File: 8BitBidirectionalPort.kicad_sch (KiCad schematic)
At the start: 4 parts

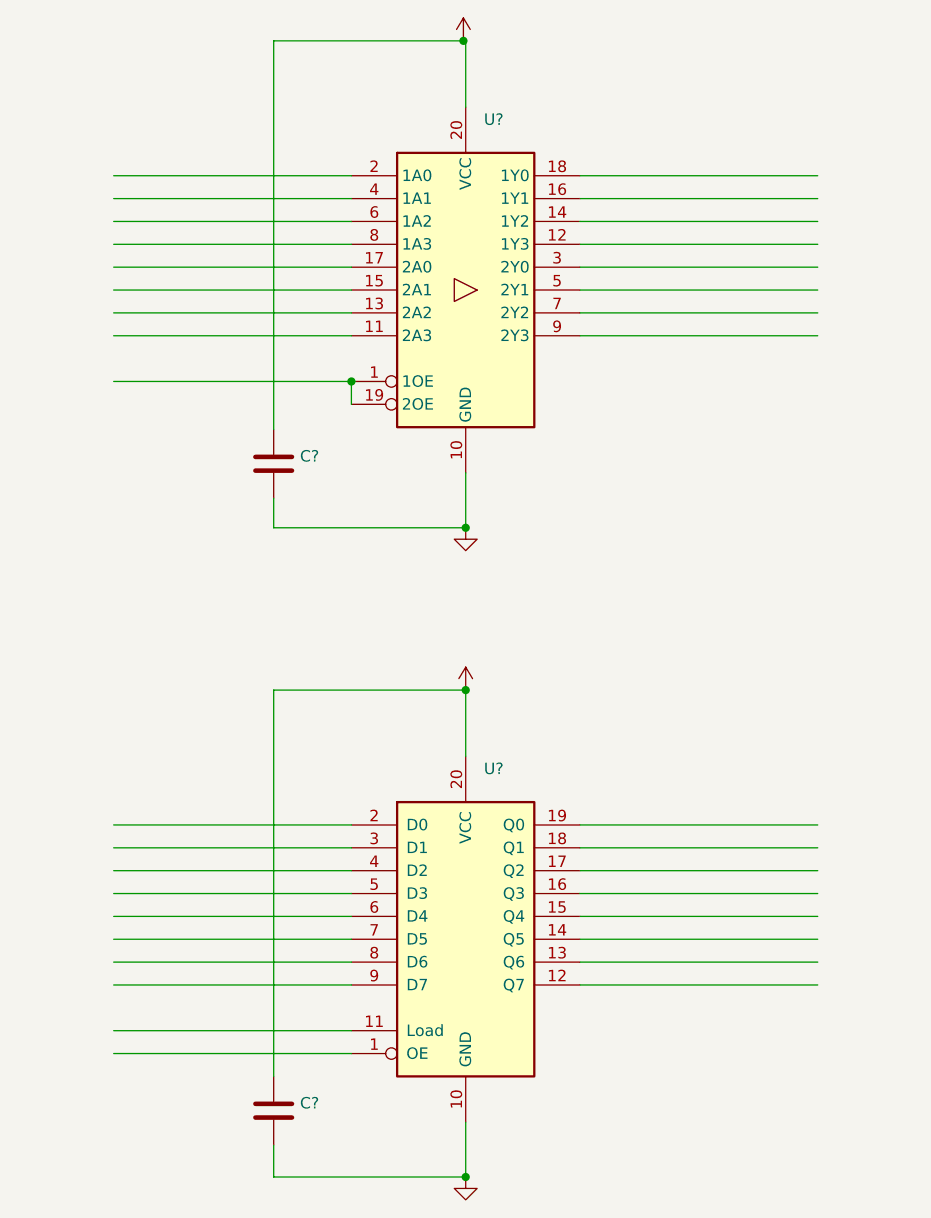
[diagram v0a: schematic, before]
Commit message: Added a 16-bit transceiver to data lines
There is no latch in this design, the GCM4 is responsible for keeping
the lines active when handling read requests from the i960. This isn't
that big of a deal. It just means that we have to keep the data line id
set for as long as possible.

This is basically what I do now for the gcm4 based boards just without
the address bits set. The data lines stay set until the next time they
need to be modified.
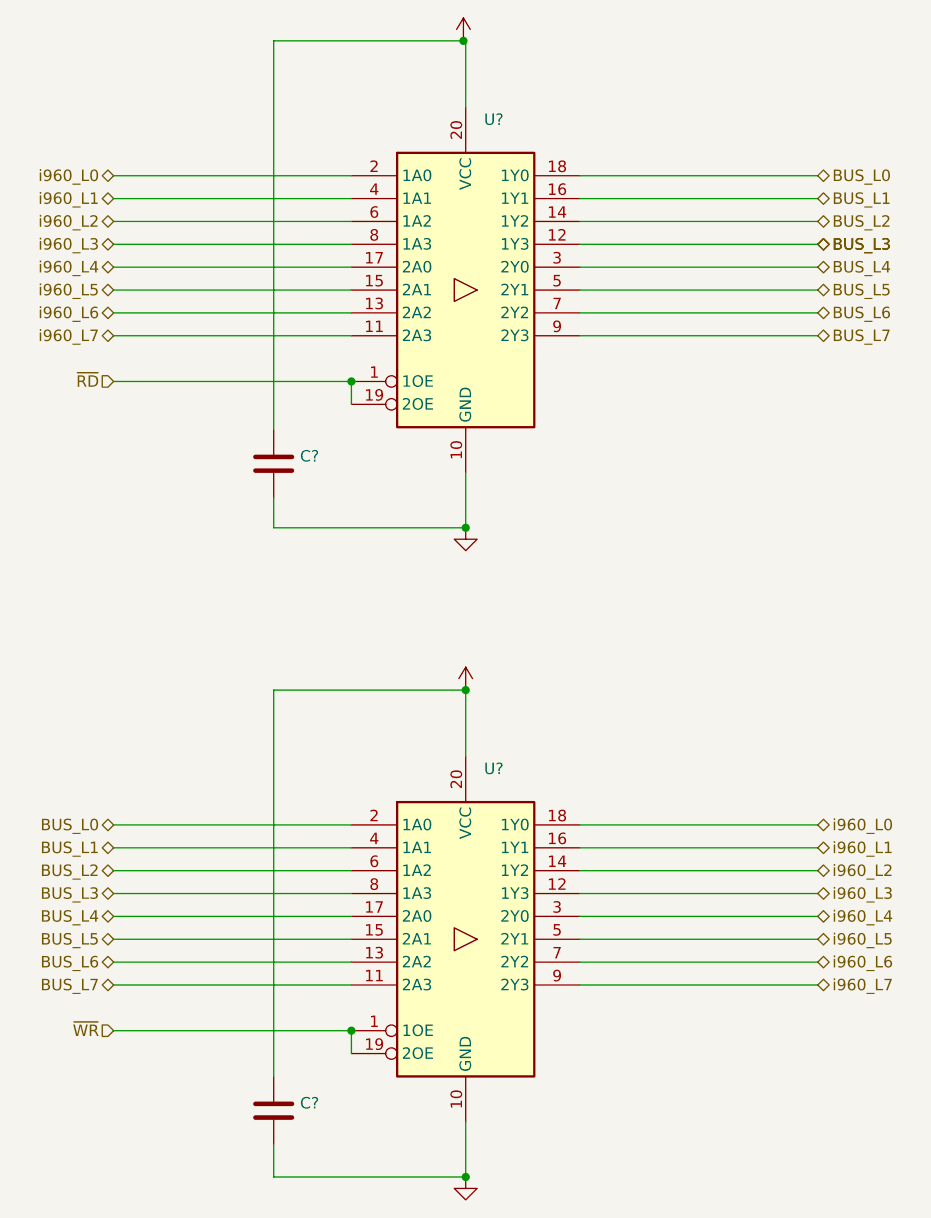
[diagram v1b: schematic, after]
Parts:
- removed U?: (no value), symbol 74xx:74LS573
- added U?: (no value), symbol 74xx:74HC244
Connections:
- net GND: now also U?.10 (GND)
- net VCC: now also U?.20 (VCC)
- net ~{RD}: now reaches U?.1 (1OE), U?.19 (2OE)
- net i960_L7: now reaches U?.11 (2A3)
- net i960_L7: now also U?.9 (2Y3)
- net BUS_L3: now reaches U?.12 (1Y3)
- net BUS_L3: now also U?.8 (1A3)
- net i960_L6: now reaches U?.13 (2A2)
- net i960_L6: now also U?.7 (2Y2)
- net BUS_L2: now reaches U?.14 (1Y2)
- net BUS_L2: now also U?.6 (1A2)
- net i960_L5: now reaches U?.15 (2A1)
- net i960_L5: now also U?.5 (2Y1)
- net BUS_L1: now reaches U?.16 (1Y1)
- net BUS_L1: now also U?.4 (1A1)
- net i960_L4: now reaches U?.17 (2A0)
- net i960_L4: now also U?.3 (2Y0)
- net BUS_L0: now reaches U?.18 (1Y0)
- net BUS_L0: now also U?.2 (1A0)
- net i960_L0: now reaches U?.2 (1A0)
- net i960_L0: now also U?.18 (1Y0)
- net BUS_L4: now reaches U?.3 (2Y0)
- net BUS_L4: now also U?.17 (2A0)
- net i960_L1: now reaches U?.4 (1A1)
- net i960_L1: now also U?.16 (1Y1)
- net BUS_L5: now reaches U?.5 (2Y1)
- net BUS_L5: now also U?.15 (2A1)
- net i960_L2: now reaches U?.6 (1A2)
- net i960_L2: now also U?.14 (1Y2)
- net BUS_L6: now reaches U?.7 (2Y2)
- net BUS_L6: now also U?.13 (2A2)
- net i960_L3: now reaches U?.8 (1A3)
- net i960_L3: now also U?.12 (1Y3)
- net BUS_L7: now reaches U?.9 (2Y3)
- net BUS_L7: now also U?.11 (2A3)
- new net ~{WR}: U?.1 (1OE), U?.19 (2OE)
